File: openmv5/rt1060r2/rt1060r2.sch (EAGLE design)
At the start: 246 parts, among them CN1 S2B-PH-K-S(LF)(SN), IC1 LM66200DRLR, IC2 TCR2LF33,LM_CT, IC3 AP61300Z6-7, IC4 IS42S16160G-6BL, IC5 IS25LP128F-JKLE-TR, IC6 ATECC608B-MAHDA-T, IC7 MXC4005XC, IC8 KSZ8081RNDCA-TR, IC9 MIMXRT106FCVL5B, J1 USB4105-GF-A, J2 USD-1040310811, J3 DF12-36-DS, J4 DNP, J5 DNP, J6 DNP, J7 DNP, J8 3221-10-0300-00, J9 DNP, M1 9774030151R, M2 9774030151R, Q1 DMG2301L-7, Q2 2N7002KW_R1_00001, Q3 2N7002KW_R1_00001, Q4 2N7002KW_R1_00001, Q5 2N7002KW_R1_00001, U1 BQ24075RGTR, U2 LBEE5KL1DX-883, Y1 ECS-327MVATX-3-CN-TR3, Y2 XRCGB24M000F3M00R0, Y3 SC32S-7PF20PPM

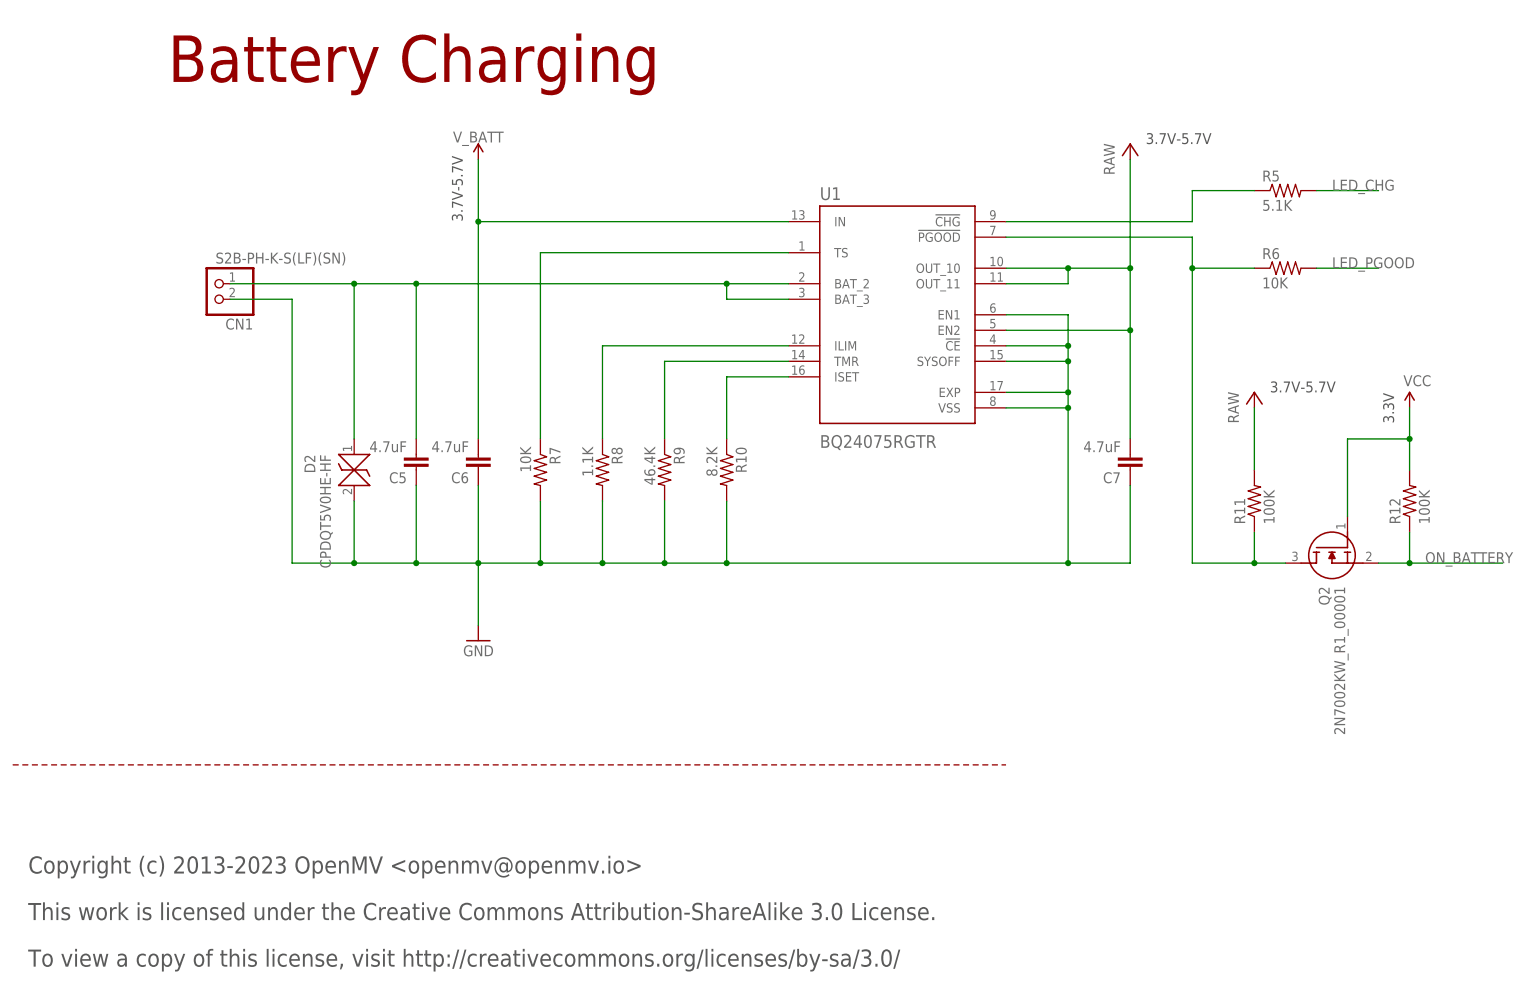
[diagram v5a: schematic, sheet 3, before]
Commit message: Make the last two I/O pins more configurable
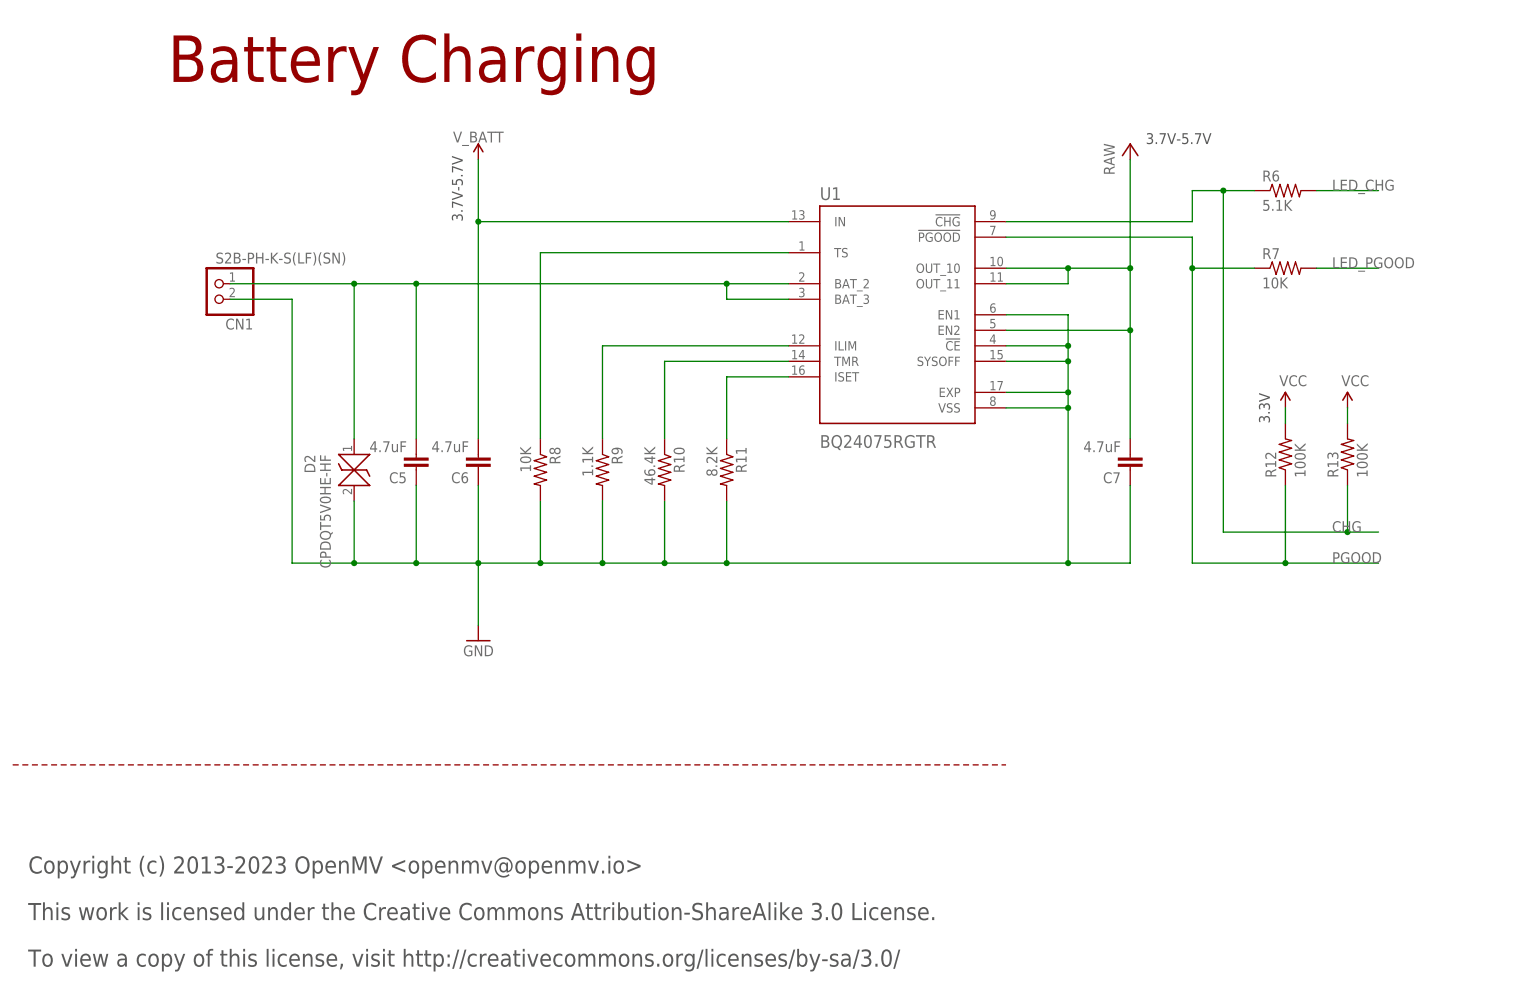
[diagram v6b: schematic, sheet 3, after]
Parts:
- removed Q5: 2N7002KW_R1_00001, 2N7002KW_R1_00001:2N7002KW_R1_00001
- added R65, R69: 100K, 0402:RES_0402
- added R66, R68: 10K, 0402:RES_0402
- added R67: 2.2M, 0402:RES_0402
- R10: value 8.2K -> 46.4K; MPN CR0402-FX-8201GLF -> WR04X4642FTL
- R11: value 100K -> 8.2K; MPN AC0402FR-07100KL -> CR0402-FX-8201GLF
- R15: value 200K -> 100K; MPN CRCW0402200KFKEDC -> AC0402FR-07100KL
- R16: value 100K -> 200K; MPN AC0402FR-07100KL -> CRCW0402200KFKEDC
- R17: value 44.2K -> 100K; MPN AC0402FR-0744K2L -> AC0402FR-07100KL
- R18: value 100K -> 44.2K; MPN AC0402FR-07100KL -> AC0402FR-0744K2L
- R20, R4: value 1K -> 100K; MPN CRCW04021K00FKEDC -> AC0402FR-07100KL
- R21: value 10K -> 1K; MPN AC0402FR-1310KL -> CRCW04021K00FKEDC
- R22: value 5.1K -> 10K; MPN RC0402JR-075K1L -> AC0402FR-1310KL
- R23, R6: value 10K -> 5.1K; MPN AC0402FR-1310KL -> RC0402JR-075K1L
- R26: value 2.7K -> 10K; MPN AC0402JR-072K7L -> AC0402FR-1310KL
- R29: value 100K -> 2.7K; MPN AC0402FR-07100KL -> AC0402JR-072K7L
- R36, R52, R61, R63: value 10K -> 100K; MPN AC0402FR-1310KL -> AC0402FR-07100KL
- R38: value 4.7K -> 10K; MPN AC0402FR-074K7L -> AC0402FR-1310KL
- R40: value 100K -> 4.7K; MPN AC0402FR-07100KL -> AC0402FR-074K7L
- R41: value 1K -> 100K; MPN AC0402FR-1310KL -> AC0402FR-07100KL
- R43: value 10K -> 1K
- R44: value 10K -> 0; MPN AC0402FR-1310KL -> RC0402JR-070RL
- R45: value DNP -> 0; MPN DNP -> RC0402JR-070RL
- R46: value DNP -> 10K; MPN DNP -> AC0402FR-1310KL
- R47, R57, R58: value 100K -> 10K; MPN AC0402FR-07100KL -> AC0402FR-1310KL
- R48: value 220 -> DNP; MPN CRGCQ0402F220R -> DNP
- R49, R51: value 1K -> DNP; MPN CRCW04021K00FKEDC -> DNP
- R5: value 5.1K -> 1K; MPN RC0402JR-075K1L -> CRCW04021K00FKEDC
- R50: value 6.49K -> DNP; MPN CR0402-FX-6491GLF -> DNP
- R53: value 10K -> 220; MPN AC0402FR-1310KL -> CRGCQ0402F220R
- R54, R56: value 100K -> 1K; MPN AC0402FR-07100KL -> CRCW04021K00FKEDC
- R55: value 100K -> 6.49K; MPN AC0402FR-07100KL -> CR0402-FX-6491GLF
- R59: value 30K -> 100K; MPN 0402WGF3002TCE -> AC0402FR-07100KL
- R62: value 2.2M -> 100K; MPN RC0402FR-072M2L -> AC0402FR-07100KL
- R64: value 100K -> 30K; MPN AC0402FR-07100KL -> 0402WGF3002TCE
- R8: value 1.1K -> 10K; MPN RC0402JR-071K1L -> AC0402FR-1310KL
- R9: value 46.4K -> 1.1K; MPN WR04X4642FTL -> RC0402JR-071K1L
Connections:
- removed net ON_BATTERY: IC9.GPIO_SD_B1_04, Q2.S, R12.1
- new net N$1: J6.3, R45.2
- new net N$2: J6.4, R44.2
- net BT_H_WAKE: now also R58.1; no longer R53.1
- net BT_REG_ON: now also R47.1; no longer R44.1
- net CHG: now also R13.1, R51.2, R6.1; no longer R5.1
- net DCDC_PSWITCH: now also R64.1; no longer R59.1
- net DCMI_D7: now also R46.1; no longer R43.1
- net DCMI_FSIN: now also R42.1; no longer R41.1
- net DCMI_PWDN: now also R38.1; no longer R37.1
- net DCMI_RST: now also R37.1; no longer R36.1
- net DCMI_SCL: now also R39.1; no longer R38.1
- net DCMI_SDA: now also R40.1; no longer R39.1
- net DCMI_SSEL: now also R36.1; no longer R35.1
- net EN: now also Q4.D, R17.1; no longer Q5.D, R16.1
- net ETH_INT: now also R54.1; no longer R49.1
- net ETH_LED: now also R53.1; no longer R48.1
- net ETH_MDIO: now also R56.1; no longer R51.1
- net ETH_RST: now also R52.1; no longer R47.1
- net FB: now also R16.1, R18.2; no longer R15.1, R17.2
- net GND: now also R11.2, R18.1, R37.2, R47.2, R55.2, R67.2; no longer R17.1, R36.2, R44.2, R50.2, R62.2, R7.2
- net ILIM: now also R9.1; no longer R8.1
- net INT_I2C_INT: now also R29.1; no longer R28.1
- net INT_I2C_SCL: now also R27.1; no longer R26.1
- net INT_I2C_SDA: now also R28.1; no longer R27.1
- net ISET: now also R11.1; no longer R10.1
- net JTAG_TDI: now also R50.1
- net JTAG_TDI_INT: now also R44.1, R48.1; no longer J6.4, R45.1
- net JTAG_TDI_INT_UNUSED: now also R48.2; no longer R45.2
- net JTAG_TRSTB: now also R51.1
- net JTAG_TRSTB_INT: now also R45.1, R49.1; no longer J6.3, R46.1
- net JTAG_TRSTB_INT_UNUSED: now also R49.2; no longer R46.2
- net LED_B: now also R21.1, R24.1; no longer R20.1, R23.1
- net LED_B_INT: now also R21.2; no longer R20.2
- net LED_CHG: now also R6.2; no longer R5.2
- net LED_G: now also R22.1, R25.1; no longer R21.1, R24.1
- net LED_G_INT: now also R22.2; no longer R21.2
- net LED_PGOOD: now also R7.2; no longer R6.2
- net LED_R: now also R23.1, R26.1; no longer R22.1, R25.1
- net LED_R_INT: now also R23.2; no longer R22.2
- net LED_ST: now also R5.2; no longer R4.2
- net MDI_LED: now also R53.2; no longer R48.2
- net ONOFF: now also Q3.S; no longer Q4.S
- net P10_PWM: now also R43.1; no longer R42.1
- net P11_WAKEUP: now also Q2.D, R14.1; no longer Q3.D, R13.1
- net P12_RST_N: now also R65.2; no longer R60.2
- net PGOOD: now also IC9.GPIO_SD_B1_04, R12.1, R7.1; no longer Q2.D, R11.1, R6.1
- net PMIC_ONOFF: now also Q3.D, R15.1; no longer Q4.D, R14.1
- net PMIC_ON_REQ: now also Q4.S; no longer Q5.S
- net PMIC_STBY_REQ: now also R69.1; no longer R64.1
- net PWM_FSIN: now also R41.1, R43.2; no longer R40.1, R41.2
- net P_FLASH_CE: now also R20.2; no longer R19.2
- net RAW: now also R15.2, R17.2; no longer D1.ANODE, R11.2, R13.2, R16.2
- net REXT: now also R55.1; no longer R50.1
- net SBL: now also R46.2; no longer R43.2
- net SDRAM_CS: now also R19.2; no longer R18.2
- net SD_CD: now also R30.1; no longer R29.1
- net SD_CMD: now also R33.1; no longer R32.1
- net SD_DAT0: now also R32.1; no longer R31.1
- net SD_DAT1: now also R31.1; no longer R30.1
- net SD_DAT2: now also R35.1; no longer R34.1
- net SD_DAT3: now also R34.1; no longer R33.1
- net ST: now also R5.1, R50.2
- net SWITCH: now also R66.1, R68.2; no longer R61.1, R63.2
- net SWITCH_OUT: now also R68.1, R69.2; no longer R63.1, R64.2
- net TMR: now also R10.1; no longer R9.1
- net TS: now also R8.1; no longer R7.1
- net VCC: now also D1.ANODE, R13.2, R16.2, R20.1, R36.2, R4.2, R41.2, R60.2, R62.2, R63.2, R64.2, R65.1, R66.2; no longer Q2.G, R15.2, R18.1, R23.2, R37.2, R47.2, R49.2, R51.2, R53.2, R55.2, R60.1
- net VDD_SNVS: now also Q2.G; no longer Q5.G
- net WAKEUP: now also Q2.S; no longer Q3.S
- net WIFI_CMD: now also R63.1; no longer R58.1
- net WIFI_D0: now also R62.1; no longer R57.1
- net WIFI_D1: now also R61.1; no longer R56.1
- net WIFI_D2: now also R60.1; no longer R55.1
- net WIFI_D3: now also R59.1; no longer R54.1
- net WL_H_WAKE: now also R57.1; no longer R52.1
- net XTALI: now also R67.1; no longer R62.1
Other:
- moved on the sheet: Q3, R10, R11, R12, R14, R16, R17, R20, R21, R22, R23, R24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

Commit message: Cleanup
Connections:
- net N$1 renamed P13
- net N$2 renamed P14
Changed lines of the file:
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@@
 </segment>
 </net>
-<net name="N$1" class="4">
+<net name="P13" class="4">
 <segment>
 <pinref part="J6" gate="G$1" pin="3"/>
@@
 </segment>
 </net>
-<net name="N$2" class="4">
+<net name="P14" class="4">
 <segment>
 <pinref part="J6" gate="G$1" pin="4"/>

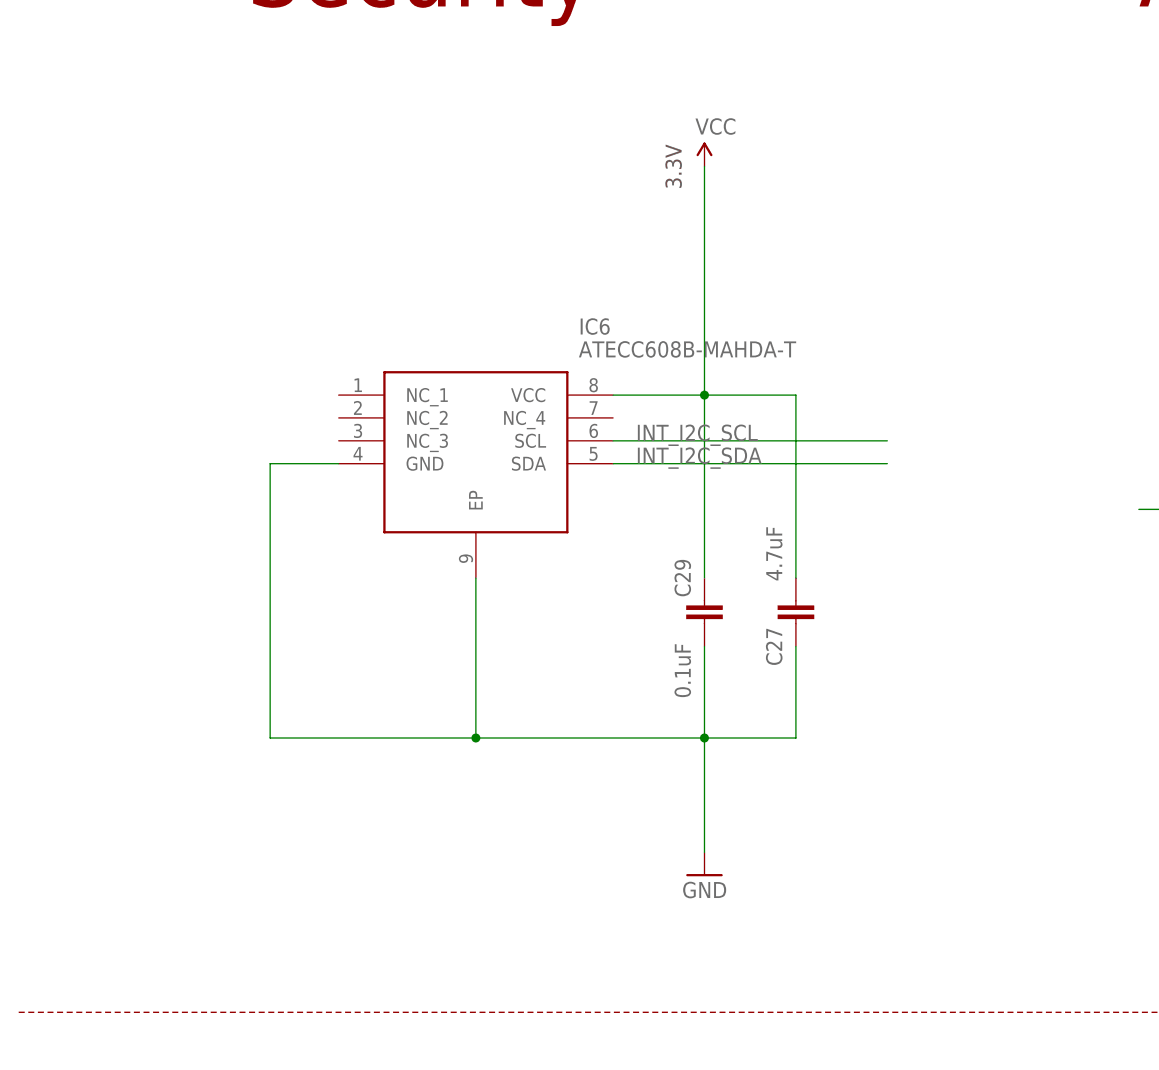
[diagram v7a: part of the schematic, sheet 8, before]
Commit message: Update the Design with the new crypto chip
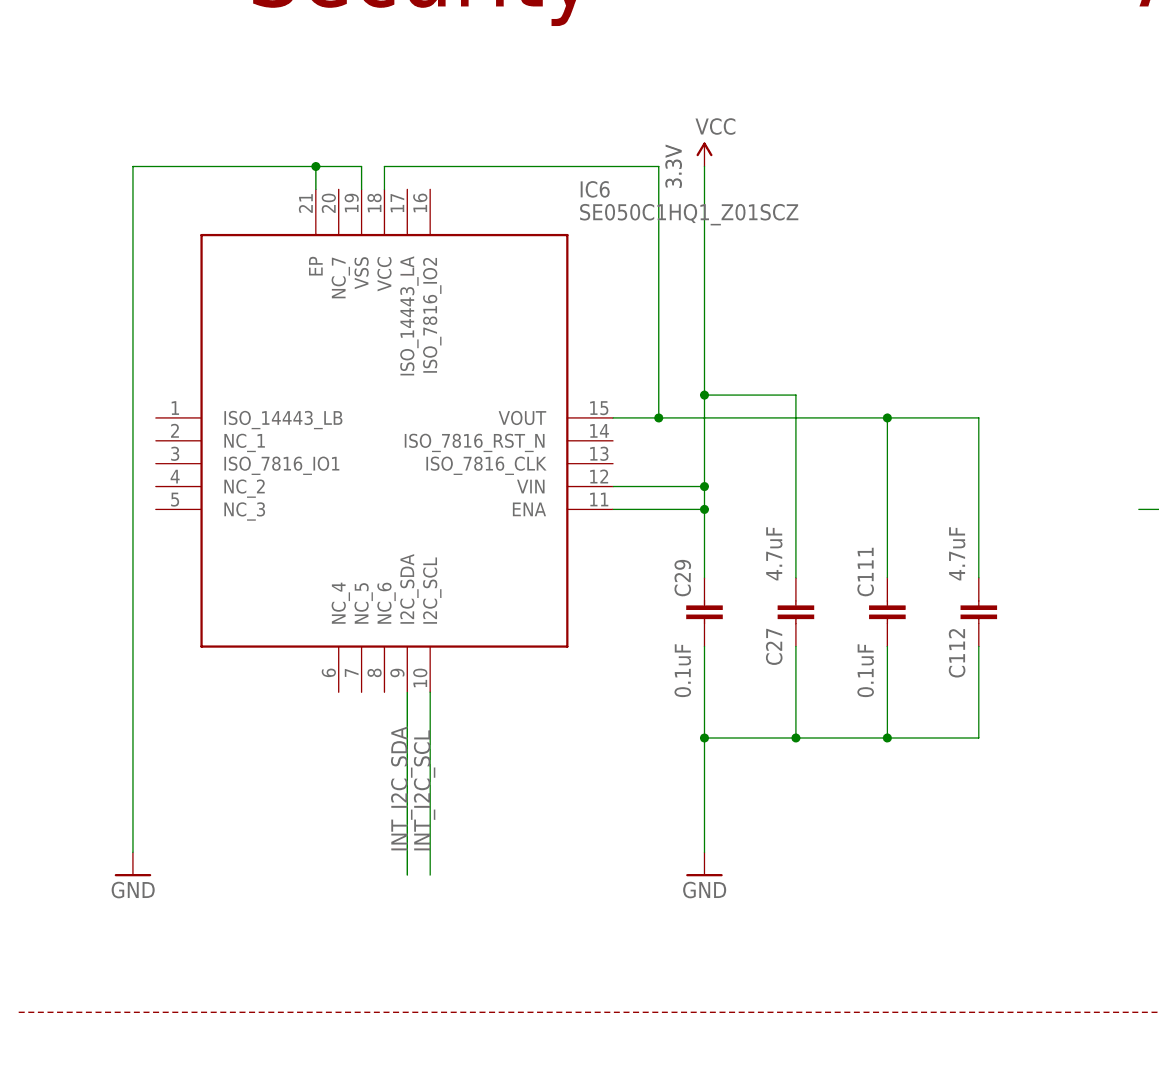
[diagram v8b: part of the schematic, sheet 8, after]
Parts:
- added C111: 0.1uF, 0402:CAP_0402
- added C112: 4.7uF, 0402:CAP_0402
- added R70: 10K, 0402:RES_0402
- added S2: KMS231GLFS, KMS231GLFS:KMS231GLFS
- IC6: value ATECC608B-MAHDA-T -> SE050C1HQ1_Z01SCZ; device ATECC608B-MAHDA-T:ATECC608B-MAHDA-T -> SE050C1HQ1_Z01SCZ:SE050C1HQ1_Z01SCZ; MPN ATECC608B-MAHDA-T -> (none)
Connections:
- new net C_VOUT: C111.1, C112.2, IC6.VCC, IC6.VOUT
- new net RST_BUTTON: R70.2, S2.COM_1, S2.COM_2, S2.COM_3
- net GND: now also C111.2, C112.1, IC6.VSS, S2.NO_1, S2.NO_2; no longer IC6.GND
- net INT_I2C_SCL: now also IC6.I2C_SCL; no longer IC6.SCL
- net INT_I2C_SDA: now also IC6.I2C_SDA; no longer IC6.SDA
- net P12_RST_N: now also R70.1
- net VCC: now also IC6.ENA, IC6.VIN; no longer IC6.VCC
